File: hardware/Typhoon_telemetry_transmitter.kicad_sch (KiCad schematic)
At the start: 18 parts, among them J1 Conn_01x04_Pin, J2 USB_C_Receptacle_USB2.0, U1 STM32F103C8Tx, U2 NRF24L01_Breakout, Y1 8M

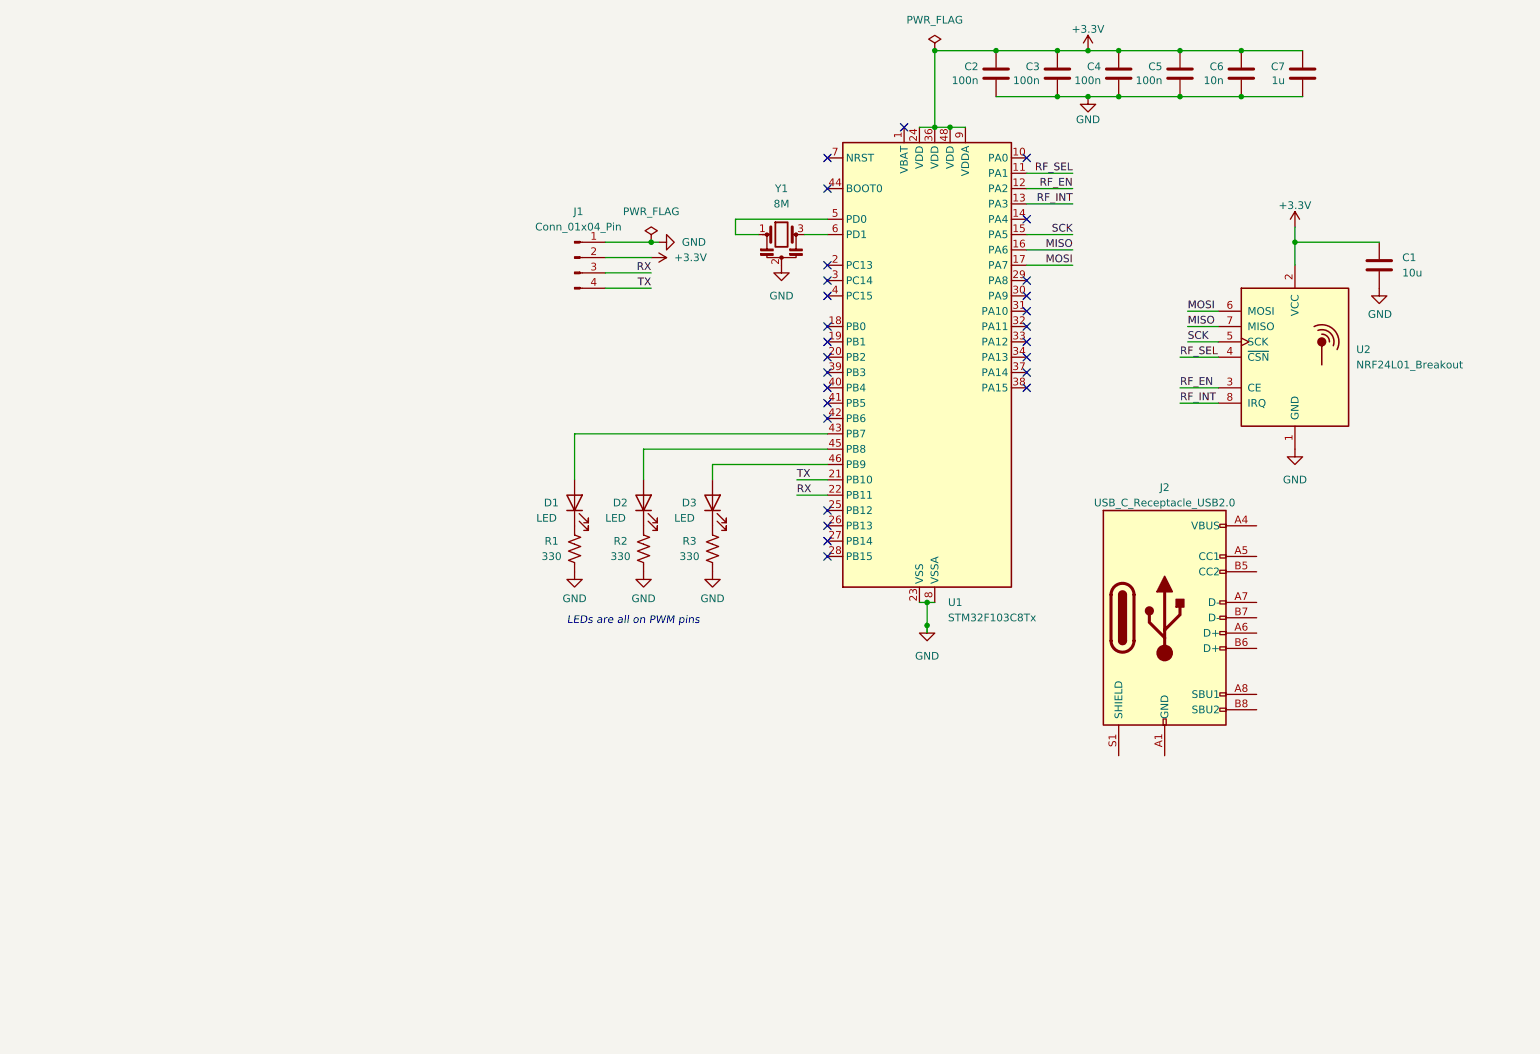
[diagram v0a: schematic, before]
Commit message: Updated debugger, pull down resistors
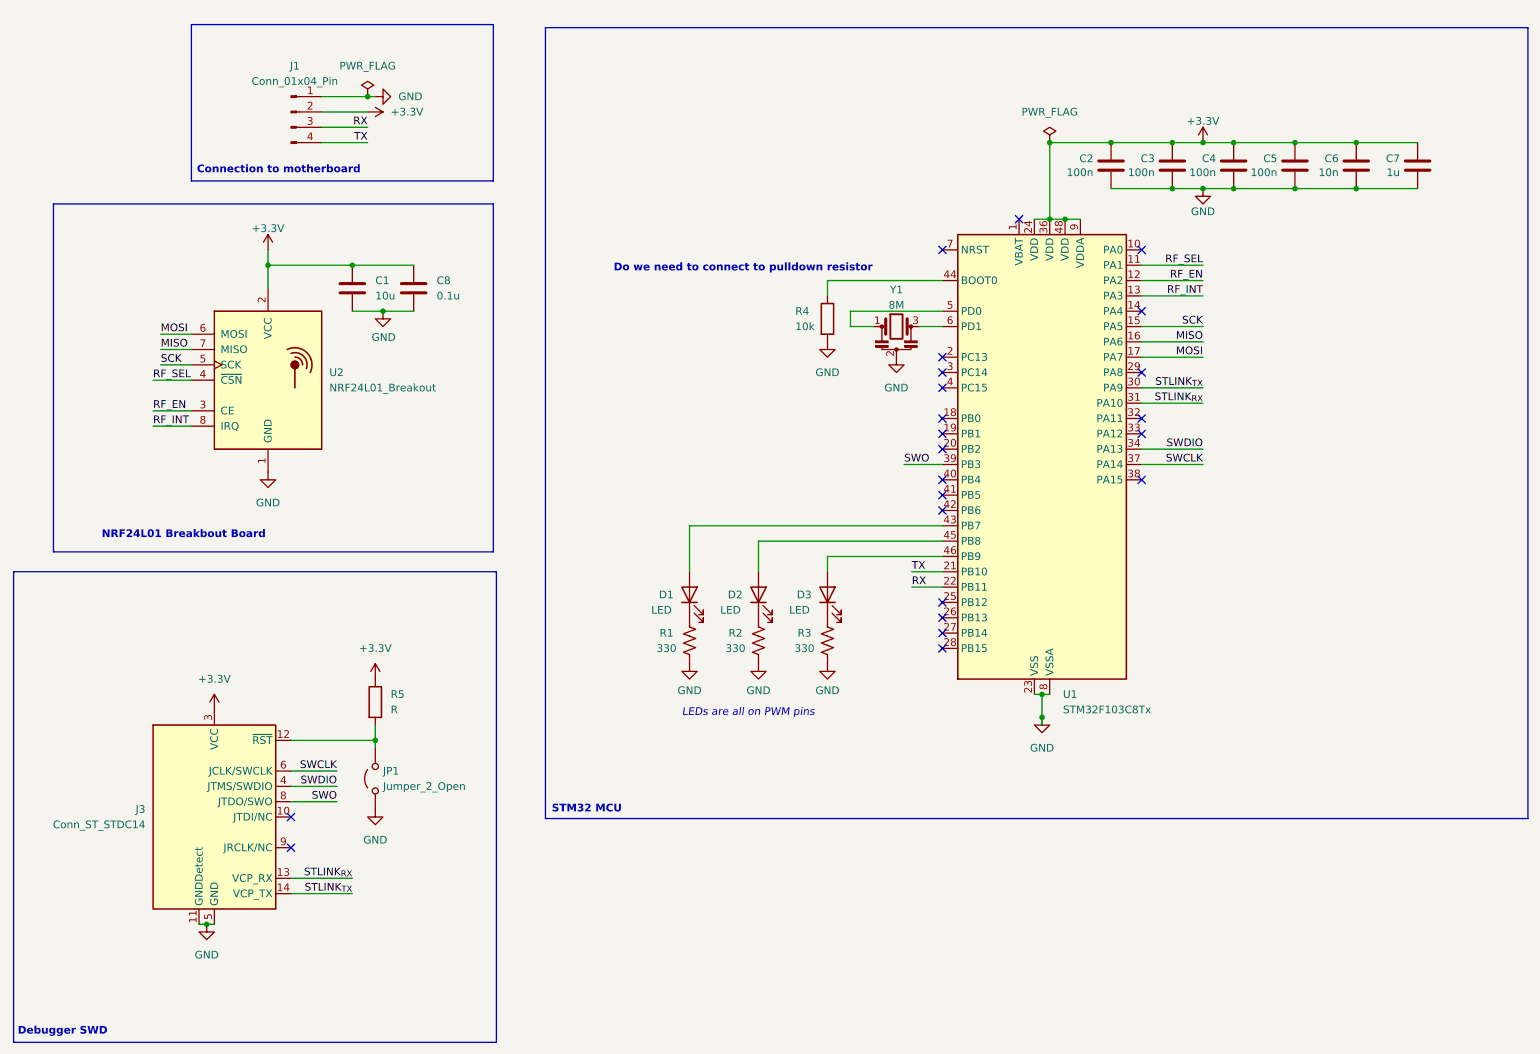
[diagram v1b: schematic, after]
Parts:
- removed J2: USB_C_Receptacle_USB2.0, Connector_USB:USB_C_Receptacle_HRO_TYPE-C-31-M-12, symbol Connector:USB_C_Receptacle_USB2.0
- added C8: 0.1u, symbol Device:C
- added J3: Conn_ST_STDC14, symbol Connector:Conn_ST_STDC14
- added JP1: Jumper_2_Open, symbol Jumper:Jumper_2_Open
- added R4: 10k, symbol Device:R
- added R5: R, symbol Device:R
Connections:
- net +3.3V: now also C8.1, J3.3 (VCC), R5.1
- net GND: now also C8.2, J3.11 (GNDDetect), J3.5 (GND), J3.7 (GND), JP1.1 (A), R4.2
- net STLINK_{TX}: now reaches U1.30 (PA9)
- net STLINK_{TX}: now also J3.14 (VCP_TX)
- net STLINK_{RX}: now reaches U1.31 (PA10)
- net STLINK_{RX}: now also J3.13 (VCP_RX)
- net SWDIO: now reaches U1.34 (PA13)
- net SWDIO: now also J3.4 (JTMS/SWDIO)
- net SWCLK: now reaches U1.37 (PA14)
- net SWCLK: now also J3.6 (JCLK/SWCLK)
- net SWO: now reaches U1.39 (PB3)
- net SWO: now also J3.8 (JTDO/SWO)
- net at U1.44 (BOOT0): now also R4.1
- new net: J3.12 (~{RST}), JP1.2 (B), R5.2
- no-connect marks 27 -> 23
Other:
- note added: "Connection to motherboard"
- note added: "Debugger SWD"
- note added: "Do we need to connect to pulldown resistor"
- note added: "NRF24L01 Breakbout Board"
- note added: "STM32 MCU"
- moved on the sheet: C1, C2, C3, C4, C5, C6, C7, D1, D2, D3, J1, R1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

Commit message: Final Final Updates
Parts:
- C8: footprint (none) -> Capacitor_SMD:C_0603_1608Metric
- J1: footprint Connector_PinHeader_1.00mm:PinHeader_1x04_P1.00mm_Vertical -> Connector_JST:JST_EH_B4B-EH-A_1x04_P2.50mm_Vertical
- J3: footprint (none) -> Connector_PinHeader_1.27mm:PinHeader_2x07_P1.27mm_Vertical_SMD
- JP1: footprint (none) -> Jumper:SolderJumper-2_P1.3mm_Open_RoundedPad1.0x1.5mm
- R4: footprint (none) -> Resistor_SMD:R_0603_1608Metric
- R5: value R -> 10k; footprint (none) -> Resistor_SMD:R_0603_1608Metric
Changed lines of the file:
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@@
 			)
 		)
-		(property "Value" "R"
+		(property "Value" "10k"
 			(at 91.44 135.8899 0)
 			(effects
@@
 			)
 		)
-		(property "Footprint" ""
+		(property "Footprint" "Resistor_SMD:R_0603_1608Metric"
 			(at 87.122 134.62 90)
 			(effects
@@
 			)
 		)
-		(property "Footprint" ""
+		(property "Footprint" "Connector_PinHeader_1.27mm:PinHeader_2x07_P1.27mm_Vertical_SMD"
 			(at 62.23 153.67 0)
 			(effects
@@
 			)
 		)
-		(property "Footprint" "Connector_PinHeader_1.00mm:PinHeader_1x04_P1.00mm_Vertical"
+		(property "Footprint" "Connector_JST:JST_EH_B4B-EH-A_1x04_P2.50mm_Vertical"
 			(at 74.93 36.83 0)
 			(effects
@@
 			)
 		)
-		(property "Footprint" ""
+		(property "Footprint" "Jumper:SolderJumper-2_P1.3mm_Open_RoundedPad1.0x1.5mm"
 			(at 88.9 147.32 0)
 			(effects
@@
 			)
 		)
-		(property "Footprint" ""
+		(property "Footprint" "Capacitor_SMD:C_0603_1608Metric"
 			(at 96.2152 69.85 0)
 			(effects
@@
 			)
 		)
-		(property "Footprint" ""
+		(property "Footprint" "Resistor_SMD:R_0603_1608Metric"
 			(at 162.052 71.12 90)
 			(effects
